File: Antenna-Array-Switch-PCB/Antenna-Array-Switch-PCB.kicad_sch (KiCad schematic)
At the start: 16 parts, among them J101 Conn_SMA, J102 Conn_SMA, J103 Conn_SMA, U101 LM1117IMP-3.3, U102 SKY13418-485LF

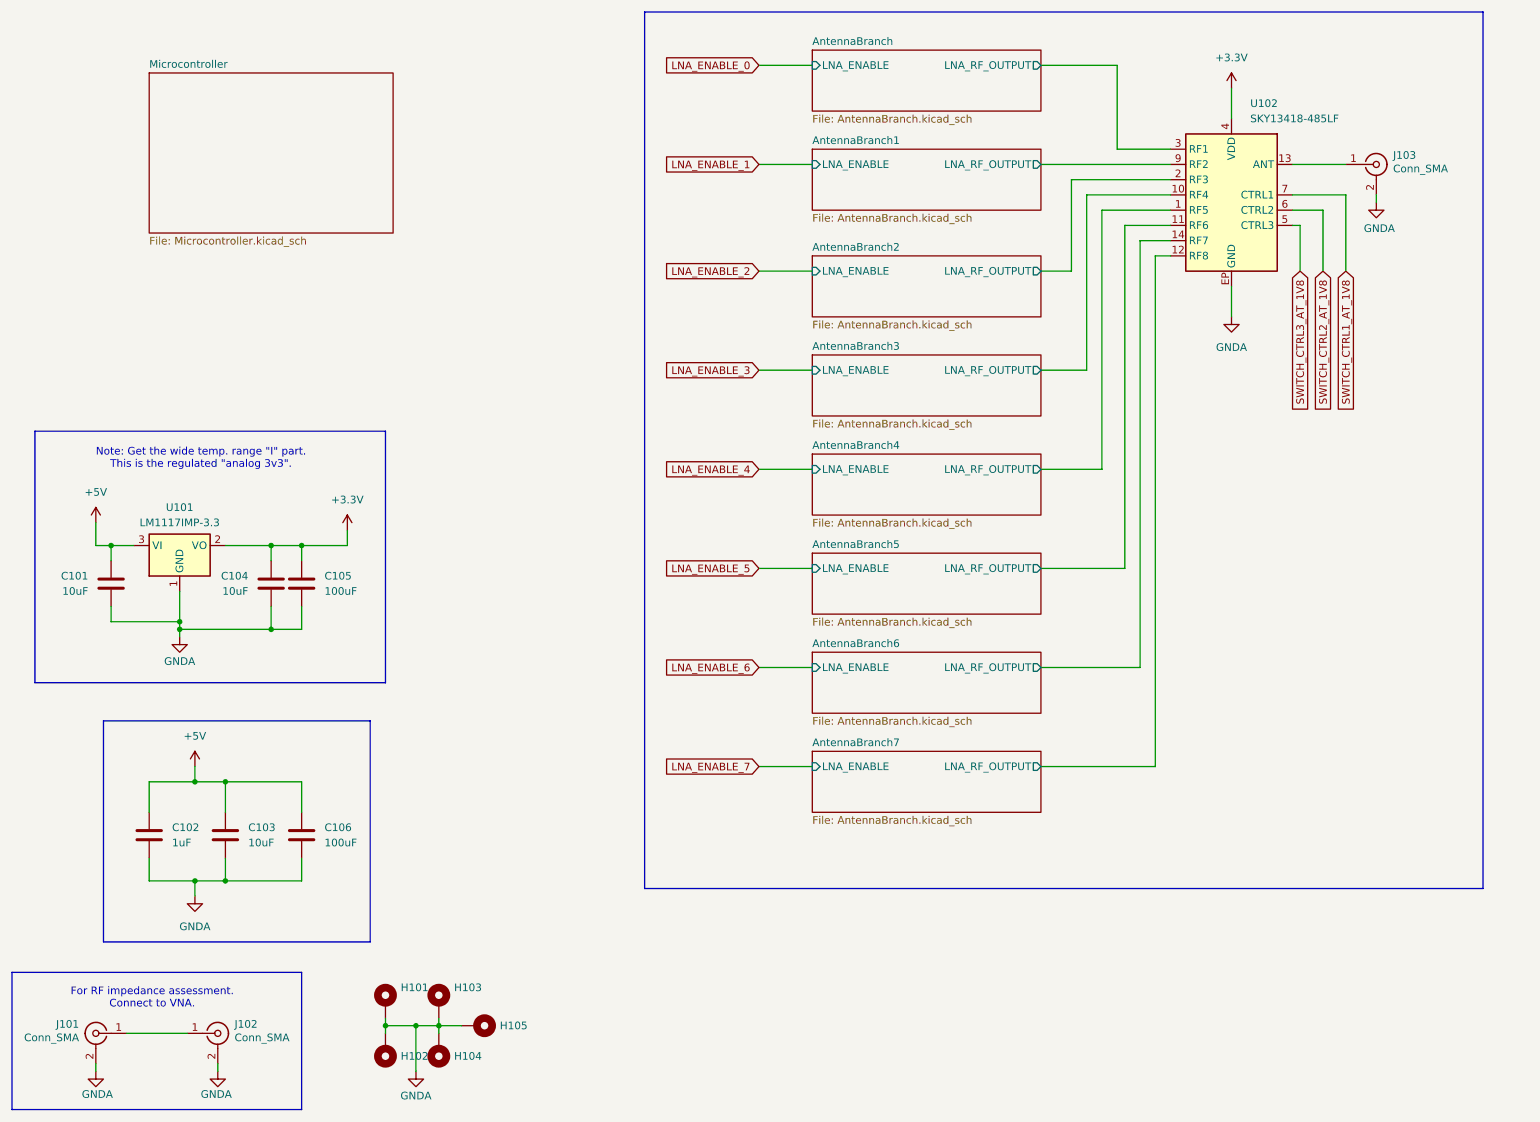
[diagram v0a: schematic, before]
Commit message: PCB Sch: Add filters at control lines
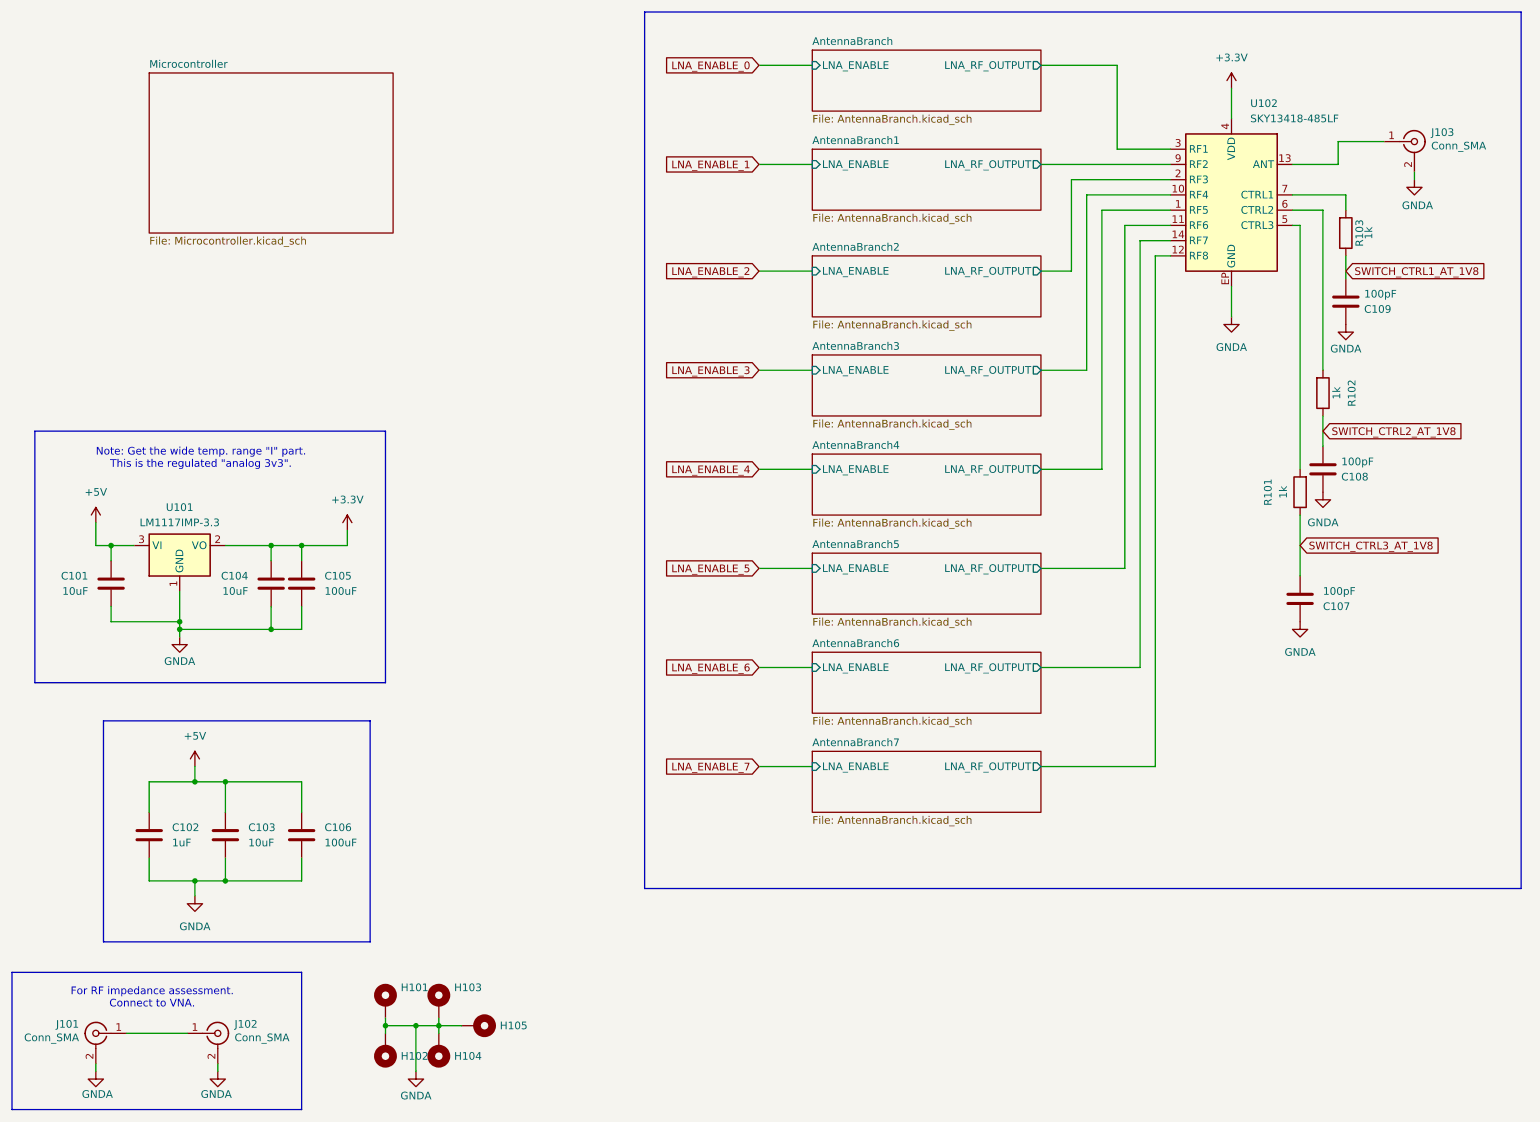
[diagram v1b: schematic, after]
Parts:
- added C107, C108, C109: 100pF, Capacitor_SMD:C_0603_1608Metric_Pad1.08x0.95mm_HandSolder, symbol Device:C
- added R101, R102, R103: 1k, Resistor_SMD:R_0603_1608Metric_Pad0.98x0.95mm_HandSolder, symbol Device:R
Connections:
- net GNDA: now also C107.2, C108.2, C109.2
- net SWITCH_CTRL1_AT_1V8: now also C109.1, R103.1; no longer U102.7 (CTRL1)
- net SWITCH_CTRL2_AT_1V8: now also C108.1, R102.1; no longer U102.6 (CTRL2)
- net SWITCH_CTRL3_AT_1V8: now also C107.1, R101.1; no longer U102.5 (CTRL3)
- new net: R102.2, U102.6 (CTRL2)
- new net: R103.2, U102.7 (CTRL1)
- new net: R101.2, U102.5 (CTRL3)
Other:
- moved on the sheet: J103

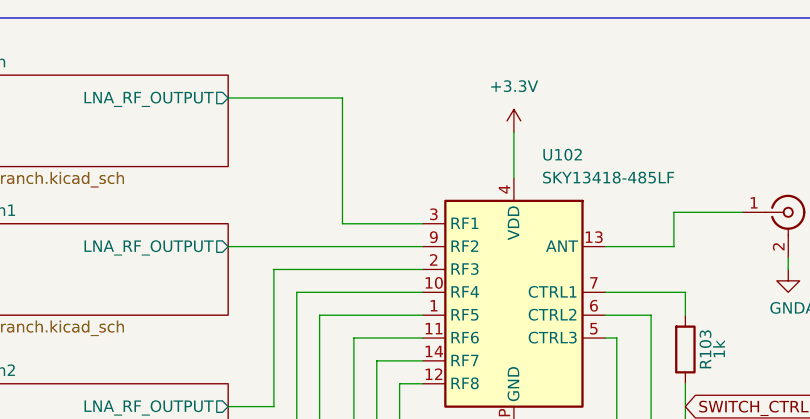
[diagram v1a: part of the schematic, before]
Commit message: PCB: More layout, legends
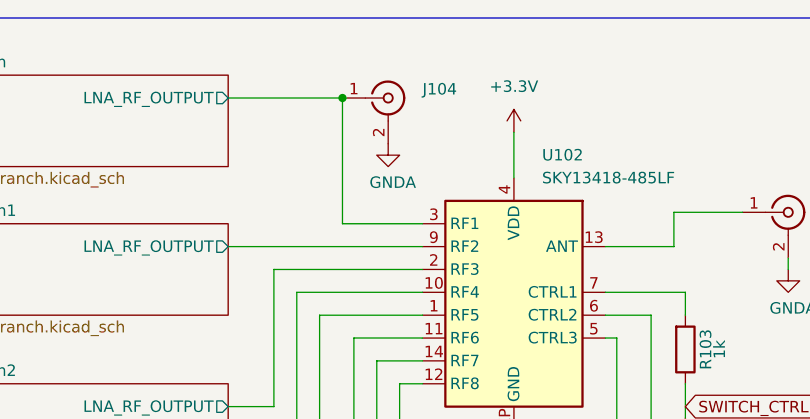
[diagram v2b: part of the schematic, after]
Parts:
- added J104: Conn_Coaxial, Connector_Coaxial:SMA_Amphenol_901-144_Vertical, symbol Connector:Conn_Coaxial
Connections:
- net AntennaBranch/LNA_RF_OUTPUT: now also J104.1 (In)
- net GNDA: now also J104.2 (Ext)
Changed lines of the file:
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@@
 	)
 	(junction
+		(at 198.12 29.21)
+		(diameter 0)
+		(color 0 0 0 0)
+	)
+	(junction
 		(at 57.15 109.22)
 		(diameter 0)
@@
 	)
 	(symbol
+		(lib_id "power:GNDA")
+		(at 203.2 34.29 0)
+		(unit 1)
+		(body_style 1)
+		(exclude_from_sim no)
+		(in_bom yes)
+		(on_board yes)
+		(in_pos_files yes)
+		(dnp no)
+		(property "Reference" "#PWR0115"
+			(at 203.2 40.64 0)
+			(hide yes)
+			(show_name no)
+			(do_not_autoplace no)
+			(effects
+				(font
+					(size 1.27 1.27)
+				)
+			)
+		)
+		(property "Value" "GNDA"
+			(at 203.708 38.608 0)
+			(show_name no)
+			(do_not_autoplace no)
+			(effects
+				(font
+					(size 1.27 1.27)
+				)
+			)
+		)
+		(property "Footprint" ""
+			(at 203.2 34.29 0)
+			(hide yes)
+			(show_name no)
+			(do_not_autoplace no)
+			(effects
+				(font
+					(size 1.27 1.27)
+				)
+			)
+		)
+		(property "Datasheet" ""
+			(at 203.2 34.29 0)
+			(hide yes)
+			(show_name no)
+			(do_not_autoplace no)
+			(effects
+				(font
+					(size 1.27 1.27)
+				)
+			)
+		)
+		(property "Description" "Power symbol creates a global label with name \"GNDA\" , analog ground"
+			(at 203.2 34.29 0)
+			(hide yes)
+			(show_name no)
+			(do_not_autoplace no)
+			(effects
+				(font
+					(size 1.27 1.27)
+				)
+			)
+		)
+		(pin "1"
+		)
+		(instances
+			(project "Antenna-Array-Switch-PCB"
+				(path "/53a2d682-f221-4d2b-9002-0fe959bb1f68"
+					(reference "#PWR0115")
+					(unit 1)
+				)
+			)
+		)
+	)
+	(symbol
 		(lib_id "Device:C")
 		(at 36.83 157.48 0)
@@
 					(unit 1)
 				)
+			)
+		)
+	)
+	(symbol
+		(lib_id "Connector:Conn_Coaxial")
+		(at 203.2 29.21 0)
+		(unit 1)
+		(body_style 1)
+		(exclude_from_sim no)
+		(in_bom yes)
+		(on_board yes)
+		(in_pos_files yes)
+		(dnp no)
+		(property "Reference" "J104"
+			(at 207.01 28.2331 0)
+			(show_name no)
+			(do_not_autoplace no)
+			(effects
+				(font
+					(size 1.27 1.27)
+				)
+				(justify left)
+			)
+		)
+		(property "Value" "Conn_Coaxial"
+			(at 207.01 30.7731 0)
+			(hide yes)
+			(show_name no)
+			(do_not_autoplace no)
+			(effects
+				(font
+					(size 1.27 1.27)
+				)
+				(justify left)
+			)
+		)
+		(property "Footprint" "Connector_Coaxial:SMA_Amphenol_901-144_Vertical"
+			(at 203.2 29.21 0)
+			(hide yes)
+			(show_name no)
+			(do_not_autoplace no)
+			(effects
+				(font
+					(size 1.27 1.27)
+				)
+			)
+		)
+		(property "Datasheet" ""
+			(at 203.2 29.21 0)
+			(hide yes)
+			(show_name no)
+			(do_not_autoplace no)
+			(effects
+				(font
+					(size 1.27 1.27)
+				)
+			)
+		)
+		(property "Description" "coaxial connector (BNC, SMA, SMB, SMC, Cinch/RCA, LEMO, ...)"
+			(at 203.2 29.21 0)
+			(hide yes)
+			(show_name no)
+			(do_not_autoplace no)
+			(effects
+				(font
+					(size 1.27 1.27)
+				)
+			)
+		)
+		(pin "2"
+		)
+		(pin "1"
+		)
+		(instances
+			(project "Antenna-Array-Switch-PCB"
+				(path "/53a2d682-f221-4d2b-9002-0fe959bb1f68"
+					(reference "J104")
+					(unit 1)
+				)

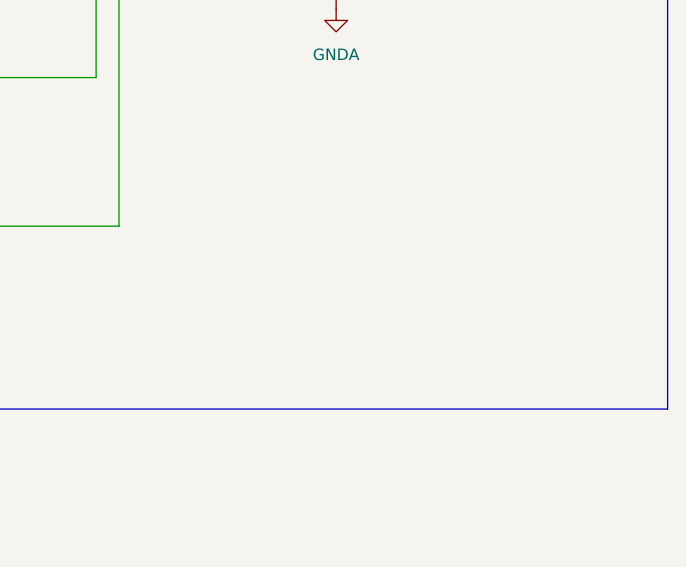
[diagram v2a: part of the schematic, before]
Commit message: PCB: Update LCSC assignments for ordering
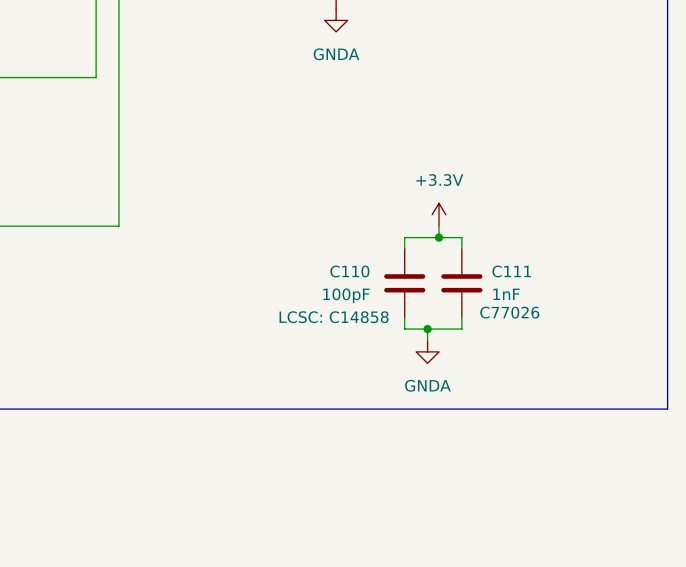
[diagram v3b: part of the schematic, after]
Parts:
- added C110: 100pF, Capacitor_SMD:C_0603_1608Metric_Pad1.08x0.95mm_HandSolder, symbol Device:C
- added C111: 1nF, Capacitor_SMD:C_0603_1608Metric_Pad1.08x0.95mm_HandSolder, symbol Device:C
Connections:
- net +3.3V: now also C110.2, C111.2
- net GNDA: now also C110.1, C111.1

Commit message: PCB: Minor updates
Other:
- note added: "TODO: Swap out for AMS1117-3.3 (JLC Basic C6186)"
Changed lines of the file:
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@@
 		)
 	)
+	(text "TODO: Swap out for AMS1117-3.3 (JLC Basic C6186)"
+		(exclude_from_sim no)
+		(at 45.72 98.044 0)
+		(effects
+			(font
+				(size 1.27 1.27)
+			)
+		)
+	)
 	(junction
 		(at 85.09 189.23)
@@
 		(in_bom no)
 		(on_board yes)
-		(in_pos_files yes)
+		(in_pos_files no)
 		(dnp no)
 		(fields_autoplaced yes)
@@
 		(in_bom no)
 		(on_board yes)
-		(in_pos_files yes)
+		(in_pos_files no)
 		(dnp no)
 		(fields_autoplaced yes)
@@
 		(in_bom no)
 		(on_board yes)
-		(in_pos_files yes)
+		(in_pos_files no)
 		(dnp no)
 		(fields_autoplaced yes)
@@
 		(in_bom no)
 		(on_board yes)
-		(in_pos_files yes)
+		(in_pos_files no)
 		(dnp no)
 		(fields_autoplaced yes)
@@
 		(in_bom no)
 		(on_board yes)
-		(in_pos_files yes)
+		(in_pos_files no)
 		(dnp no)
 		(fields_autoplaced yes)
